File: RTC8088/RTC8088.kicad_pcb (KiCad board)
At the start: 2 copper layers, 88 x 38.1 mm, 7 parts, among them J1 CMOS CLEAR, J2 IRQ, U1 DS12885, U2 ATF16V8B, X1 32768Hz

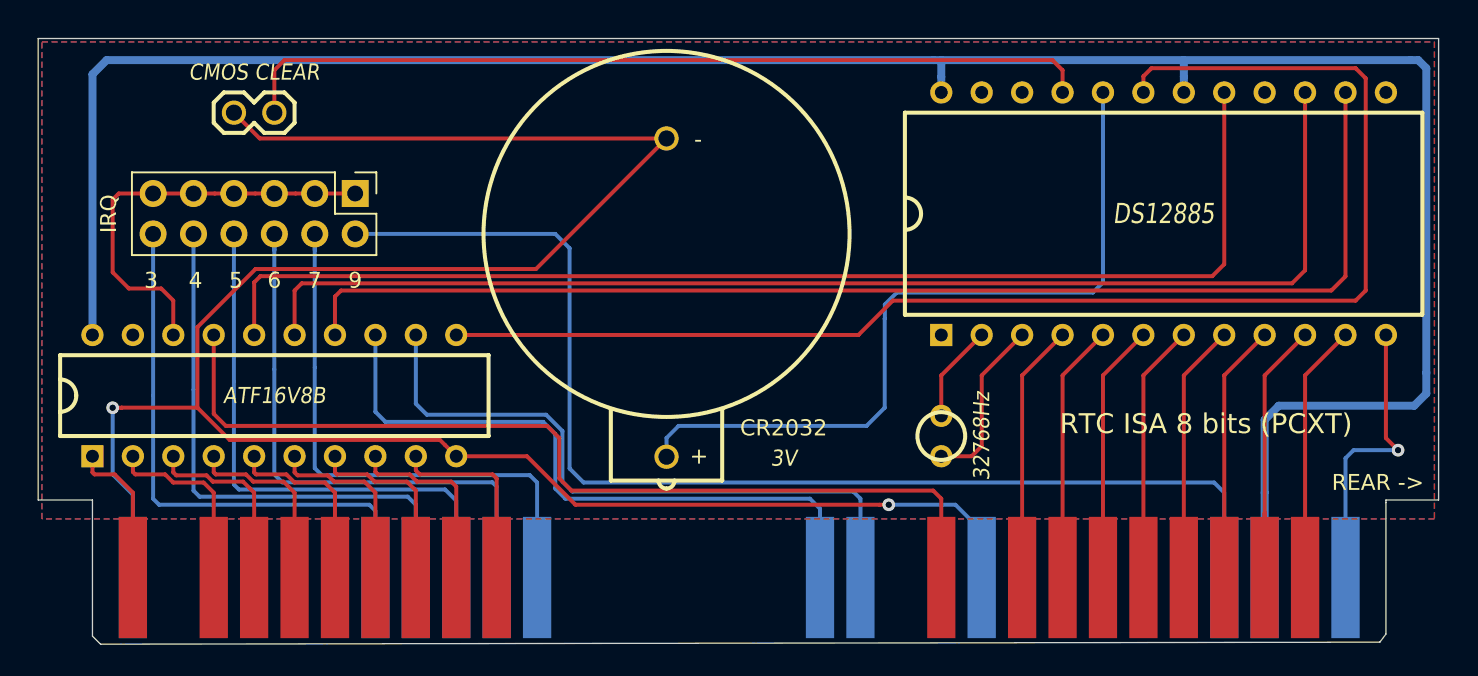
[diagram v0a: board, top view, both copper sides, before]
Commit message: v1.2
Diode is added between GND and VBAT for correct detection of absence of battery.
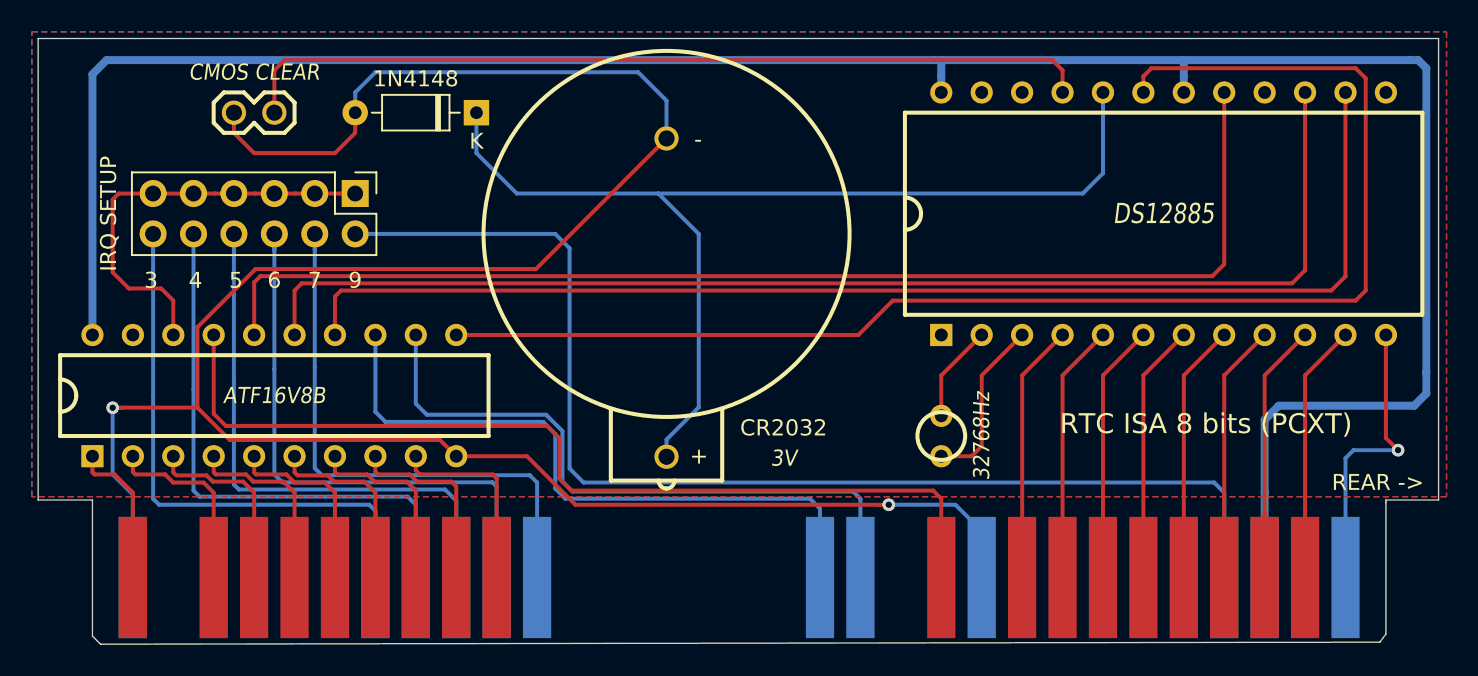
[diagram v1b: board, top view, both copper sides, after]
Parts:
- added D1: 1N4148, Diode_THT:D_DO-35_SOD27_P7.62mm_Horizontal, F.Cu at (129.5, 73.7)
- J2: value IRQ -> IRQ SETUP
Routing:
- net Net-(CR2032-Pad1): track 48.4 -> 67.0 mm
- net GND: track 157.8 -> 165.6 mm
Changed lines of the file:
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@@
     (thickness 1.6)
     (drawings 22)
-    (tracks 263)
+    (tracks 270)
     (zones 0)
-    (modules 7)
+    (modules 8)
     (nets 42)
   )
@@
     (add_net "Net-(U2-Pad19)")
   )
+  (module Diode_THT:D_DO-35_SOD27_P7.62mm_Horizontal (layer F.Cu)
+    (at 129.54 73.66 180)
+    (descr "Diode, DO-35_SOD27 series, Axial, Horizontal, pin pitch=7.62mm, , length*diameter=4*2mm^2, , http://www.diodes.com/_files/packages/DO-35.pdf")
+    (tags "Diode DO-35_SOD27 series Axial Horizontal pin pitch 7.62mm  length 4mm diameter 2mm")
+    (fp_text reference D1 (at 3.81 -2.12) (layer F.SilkS) hide
+      (effects (font (size 1 1) (thickness 0.15)))
+    )
+    (fp_text value 1N4148 (at 3.81 2.12) (layer F.SilkS)
+      (effects (font (size 1 1) (thickness 0.15)))
+    )
+    (fp_text user K (at 0 -1.8) (layer F.SilkS)
+      (effects (font (size 1 1) (thickness 0.15)))
+    )
+    (fp_text user K (at 0 -1.8) (layer F.Fab)
+      (effects (font (size 1 1) (thickness 0.15)))
+    )
+    (fp_text user %R (at 4.11 0) (layer F.Fab)
+      (effects (font (size 0.8 0.8) (thickness 0.12)))
+    )
+    (fp_line (start 8.67 -1.25) (end -1.05 -1.25) (layer F.CrtYd) (width 0.05))
+    (fp_line (start 8.67 1.25) (end 8.67 -1.25) (layer F.CrtYd) (width 0.05))
+    (fp_line (start -1.05 1.25) (end 8.67 1.25) (layer F.CrtYd) (width 0.05))
+    (fp_line (start -1.05 -1.25) (end -1.05 1.25) (layer F.CrtYd) (width 0.05))
+    (fp_line (start 2.29 -1.12) (end 2.29 1.12) (layer F.SilkS) (width 0.12))
+    (fp_line (start 2.53 -1.12) (end 2.53 1.12) (layer F.SilkS) (width 0.12))
+    (fp_line (start 2.41 -1.12) (end 2.41 1.12) (layer F.SilkS) (width 0.12))
+    (fp_line (start 6.58 0) (end 5.93 0) (layer F.SilkS) (width 0.12))
+    (fp_line (start 1.04 0) (end 1.69 0) (layer F.SilkS) (width 0.12))
+    (fp_line (start 5.93 -1.12) (end 1.69 -1.12) (layer F.SilkS) (width 0.12))
+    (fp_line (start 5.93 1.12) (end 5.93 -1.12) (layer F.SilkS) (width 0.12))
+    (fp_line (start 1.69 1.12) (end 5.93 1.12) (layer F.SilkS) (width 0.12))
+    (fp_line (start 1.69 -1.12) (end 1.69 1.12) (layer F.SilkS) (width 0.12))
+    (fp_line (start 2.31 -1) (end 2.31 1) (layer F.Fab) (width 0.1))
+    (fp_line (start 2.51 -1) (end 2.51 1) (layer F.Fab) (width 0.1))
+    (fp_line (start 2.41 -1) (end 2.41 1) (layer F.Fab) (width 0.1))
+    (fp_line (start 7.62 0) (end 5.81 0) (layer F.Fab) (width 0.1))
+    (fp_line (start 0 0) (end 1.81 0) (layer F.Fab) (width 0.1))
+    (fp_line (start 5.81 -1) (end 1.81 -1) (layer F.Fab) (width 0.1))
+    (fp_line (start 5.81 1) (end 5.81 -1) (layer F.Fab) (width 0.1))
+    (fp_line (start 1.81 1) (end 5.81 1) (layer F.Fab) (width 0.1))
+    (fp_line (start 1.81 -1) (end 1.81 1) (layer F.Fab) (width 0.1))
+    (pad 2 thru_hole oval (at 7.62 0 180) (size 1.6 1.6) (drill 0.8) (layers *.Cu *.Mask)
+      (net 1 GND))
+    (pad 1 thru_hole rect (at 0 0 180) (size 1.6 1.6) (drill 0.8) (layers *.Cu *.Mask)
+      (net 3 "Net-(CR2032-Pad1)"))
+    (model ${KISYS3DMOD}/Diode_THT.3dshapes/D_DO-35_SOD27_P7.62mm_Horizontal.wrl
+      (at (xyz 0 0 0))
+      (scale (xyz 1 1 1))
+      (rotate (xyz 0 0 0))
+    )
+  )
   (module SergeyLibraries:IC_DIP20_300 (layer F.Cu)
     (at 116.84 91.44)
@@
       (effects (font (size 1 1) (thickness 0.15)))
     )
-    (fp_text value IRQ (at 1.27 15.494 90) (layer F.SilkS)
+    (fp_text value "IRQ SETUP" (at 1.27 15.494 90) (layer F.SilkS)
       (effects (font (size 1 1) (thickness 0.15)))
     )
@@
   (segment (start 115.659247 83.485971) (end 112.006499 87.138719) (width 0.25) (layer F.Cu) (net 1))
   (segment (start 141.484806 75.28052) (end 133.279355 83.485971) (width 0.25) (layer F.Cu) (net 1))
-  (segment (start 115.92052 75.28052) (end 114.3 73.66) (width 0.25) (layer F.Cu) (net 1))
-  (segment (start 141.484806 75.28052) (end 115.92052 75.28052) (width 0.25) (layer F.Cu) (net 1))
   (segment (start 106.68 96.393) (end 106.68 92.202) (width 0.25) (layer B.Cu) (net 1))
   (segment (start 107.95 102.87) (end 107.95 97.663) (width 0.25) (layer B.Cu) (net 1))
@@
   (segment (start 186.69 94.107) (end 186.69 87.63) (width 0.25) (layer F.Cu) (net 1))
   (segment (start 187.452 94.869) (end 186.69 94.107) (width 0.25) (layer F.Cu) (net 1))
+  (segment (start 121.92 73.66) (end 121.92 74.93) (width 0.25) (layer F.Cu) (net 1))
+  (segment (start 121.92 74.93) (end 120.65 76.2) (width 0.25) (layer F.Cu) (net 1))
+  (segment (start 120.65 76.2) (end 115.57 76.2) (width 0.25) (layer F.Cu) (net 1))
+  (segment (start 115.57 76.2) (end 114.3 74.93) (width 0.25) (layer F.Cu) (net 1))
+  (segment (start 114.3 74.93) (end 114.3 73.66) (width 0.25) (layer F.Cu) (net 1))
+  (segment (start 141.484806 75.28052) (end 141.484806 72.904806) (width 0.25) (layer B.Cu) (net 1))
+  (segment (start 141.484806 72.904806) (end 139.7 71.12) (width 0.25) (layer B.Cu) (net 1))
+  (segment (start 139.7 71.12) (end 123.19 71.12) (width 0.25) (layer B.Cu) (net 1))
+  (segment (start 123.19 71.12) (end 121.92 72.39) (width 0.25) (layer B.Cu) (net 1))
+  (segment (start 121.92 72.39) (end 121.92 73.66) (width 0.25) (layer B.Cu) (net 1))
   (segment (start 106.299 70.358) (end 158.242 70.358) (width 0.5) (layer B.Cu) (net 2))
   (segment (start 105.41 87.63) (end 105.41 71.247) (width 0.5) (layer B.Cu) (net 2))
@@
   (segment (start 179.07 92.964) (end 179.07 97.536) (width 0.5) (layer B.Cu) (net 2))
   (segment (start 179.959 92.075) (end 179.07 92.964) (width 0.5) (layer B.Cu) (net 2))
-  (segment (start 168.275 84.963) (end 168.91 84.328) (width 0.25) (layer B.Cu) (net 3))
-  (segment (start 155.956 84.963) (end 168.275 84.963) (width 0.25) (layer B.Cu) (net 3))
-  (segment (start 155.201501 86.606499) (end 155.201501 85.717499) (width 0.25) (layer B.Cu) (net 3))
-  (segment (start 141.484806 94.100194) (end 142.24 93.345) (width 0.25) (layer B.Cu) (net 3))
-  (segment (start 155.201501 85.717499) (end 155.956 84.963) (width 0.25) (layer B.Cu) (net 3))
-  (segment (start 141.484806 95.28048) (end 141.484806 94.100194) (width 0.25) (layer B.Cu) (net 3))
-  (segment (start 168.91 84.328) (end 168.91 72.39) (width 0.25) (layer B.Cu) (net 3))
-  (segment (start 154.051 93.345) (end 155.194 92.202) (width 0.25) (layer B.Cu) (net 3))
-  (segment (start 142.24 93.345) (end 154.051 93.345) (width 0.25) (layer B.Cu) (net 3))
-  (segment (start 155.194 92.202) (end 155.194 86.614) (width 0.25) (layer B.Cu) (net 3))
-  (segment (start 155.194 86.614) (end 155.201501 86.606499) (width 0.25) (layer B.Cu) (net 3))
+  (segment (start 129.54 73.66) (end 129.54 76.2) (width 0.25) (layer B.Cu) (net 3))
+  (segment (start 129.54 76.2) (end 132.08 78.74) (width 0.25) (layer B.Cu) (net 3))
+  (segment (start 167.64 78.74) (end 168.91 77.47) (width 0.25) (layer B.Cu) (net 3))
+  (segment (start 168.91 77.47) (end 168.91 72.39) (width 0.25) (layer B.Cu) (net 3))
+  (segment (start 141.484806 94.20285) (end 143.51 92.177656) (width 0.25) (layer B.Cu) (net 3))
+  (segment (start 141.484806 95.28048) (end 141.484806 94.20285) (width 0.25) (layer B.Cu) (net 3))
+  (segment (start 143.51 81.28) (end 140.97 78.74) (width 0.25) (layer B.Cu) (net 3))
+  (segment (start 143.51 92.177656) (end 143.51 81.28) (width 0.25) (layer B.Cu) (net 3))
+  (segment (start 132.08 78.74) (end 140.97 78.74) (width 0.25) (layer B.Cu) (net 3))
+  (segment (start 140.97 78.74) (end 167.64 78.74) (width 0.25) (layer B.Cu) (net 3))
   (segment (start 166.37 70.993) (end 166.37 72.39) (width 0.25) (layer F.Cu) (net 4))
   (segment (start 165.735 70.358) (end 166.37 70.993) (width 0.25) (layer F.Cu) (net 4))
@@
   (segment (start 185.42 84.836) (end 185.42 71.501) (width 0.25) (layer F.Cu) (net 41))
   (segment (start 185.42 71.501) (end 184.785 70.866) (width 0.25) (layer F.Cu) (net 41))
+  (zone (net 1) (net_name GND) (layer B.Cu) (hatch edge 0.508)
+    (connect_pads (clearance 0.508))
+    (min_thickness 0.254)
+    (fill yes (arc_segments 32) (thermal_gap 0.508) (thermal_bridge_width 0.508))
+    (polygon
+      (pts
+        (xy 101.6 68.58) (xy 190.5 68.58) (xy 190.5 97.79) (xy 101.6 97.79)
+      )
+    )
+  )
   (zone (net 1) (net_name GND) (layer F.Cu) (hatch edge 0.508)
     (connect_pads (clearance 0.508))
@@
     (polygon
       (pts
-        (xy 102.235 69.215) (xy 189.738 69.215) (xy 189.738 99.187) (xy 102.235 99.187)
+        (xy 101.6 68.58) (xy 190.5 68.58) (xy 190.5 97.79) (xy 101.6 97.79)
       )
     )
-  )
-  (zone (net 1) (net_name GND) (layer B.Cu) (hatch edge 0.508)
-    (connect_pads (clearance 0.508))
-    (min_thickness 0.254)
-    (fill yes (arc_segments 32) (thermal_gap 0.508) (thermal_bridge_width 0.508))
-    (polygon
-      (pts
-        (xy 102.235 69.215) (xy 189.738 69.215) (xy 189.738 99.187) (xy 102.235 99.187)
-      )
-    )
